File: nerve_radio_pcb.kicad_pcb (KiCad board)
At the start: 4 copper layers, 50 x 50 mm, 24 parts, among them J1 BF030-20A-B1-0360-0277-0600-LB, J2 5V GPIO Breakout, J3 3V SPI Breakout, U1 TXB0104QPWRQ1, U2 TPSM82903, U3 XBP9B-DMWT-002

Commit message: Major cleanup
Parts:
- moved J3 3.20 mm to (126.0, 103.0)
- moved U1 0.40 mm to (164.6, 106.9)
- moved J2 0.32 mm to (171.0, 109.0)
- moved TP1 0.25 mm to (169.0, 90.5)
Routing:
- net /GPIO_2/PWM_2: track 36.0 -> 33.5 mm
- net /GPIO_1/PWM_1: track 31.3 -> 28.9 mm
- net /SPI_CLK: track 24.9 -> 26.9 mm
- net /SPI_CS: track 19.2 -> 21.0 mm
- net /SPI_MOSI: track 23.3 -> 24.7 mm
- net /GPIO_2/PWM_2_{5V}: track 8.94 -> 9.75 mm
- net /SPI_MISO: track 26.6 -> 27.3 mm
- net /GPIO_1/PWM_1_{5V}: track 7.20 -> 7.89 mm
- net +5V: track 34.8 -> 35.5 mm
- net GND: vias 129 -> 121
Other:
- board text added: "3.3V"
- board text added: "5V"
- board text added: "CLK"
- board text added: "CS"
- board text added: "GND"
- board text added: "MISO"
- board text added: "MOSI"
- board text added: "PWM1_{5V}"
- board text added: "PWM2_{5V}"

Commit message: Cleanup and add battery connector
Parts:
- added J4: Battery, radio_pcb_connectors:battery, F.Cu at (167.5, 99.5)
- moved C1 2.20 mm to (163.1, 95.8)
- moved C3 2.20 mm to (168.8, 93.9)
- moved R1 2.20 mm to (166.8, 89.8)
- moved R2 2.20 mm to (166.8, 95.4)
- moved TP1 2.20 mm to (171.0, 91.4)
- moved U2 2.20 mm to (165.2, 92.5)
- moved J2 2.00 mm to (171.0, 111.0)
- moved C2 1.98 mm to (162.0, 91.0)
- moved U1 1.95 mm to (164.6, 108.8)
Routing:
- net +5V: track 35.5 -> 10.9 mm, vias 7 -> 13
- net +3V3: track 21.2 -> 18.6 mm, vias 9 -> 7
- net GND: track 10.0 -> 12.5 mm, vias 121 -> 123
- net /GPIO_2/PWM_2: track 33.5 -> 35.3 mm
- net /GPIO_1/PWM_1: track 28.9 -> 30.6 mm
- net /RADIO_UART_RX: track 26.6 -> 28.1 mm
- net /RADIO_UART_TX: track 27.9 -> 28.7 mm
- net +VSUPPLY: vias 0 -> 7
- added copper zone on F.Cu, net +3V3
- added copper zone on B.Cu, net +VSUPPLY
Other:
- board text added: "BAT+"
- board text added: "J4"

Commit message: Cleanup silkscreen
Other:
- board text added: "Daniel Jeon nerve_radio_pcb v0.1.0-alpha"
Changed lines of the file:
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@@
 	)
 	(gr_text "GND"
-		(at 172.25 99.5 90)
+		(at 172.25 99.5 -90)
 		(layer "B.SilkS" knockout)
 		(effects
@@
 	)
 	(gr_text "BAT+"
-		(at 162.75 99.5 90)
+		(at 162.75 99.5 -90)
 		(layer "B.SilkS" knockout)
 		(effects
@@
 		)
 	)
+	(gr_text "Daniel Jeon\nnerve_radio_pcb\nv0.1.0-alpha"
+		(at 148.5 128.75 0)
+		(layer "B.SilkS")
+		(effects
+			(font
+				(size 1 1)
+				(thickness 0.2)
+				(bold yes)
+			)
+			(justify bottom mirror)
+		)
+	)
 	(gr_text "3.3V"
 		(at 127.75 103 0)
@@
 	)
 	(gr_text "BAT+"
-		(at 162.75 99.5 90)
+		(at 162.75 99.5 -90)
 		(layer "F.SilkS" knockout)
 		(effects
@@
 	)
 	(gr_text "GND"
-		(at 172.25 99.5 90)
+		(at 172.25 99.5 -90)
 		(layer "F.SilkS" knockout)
 		(effects
@@
 	)
 	(via
-		(at 151 127.5)
+		(at 151.25 127.5)
 		(size 0.9)
 		(drill 0.4)
@@
 	)
 	(via
-		(at 146 127.5)
-		(size 0.9)
-		(drill 0.4)
+		(at 145.75 127.5)
+		(size 0.9)
+		(drill 0.4)

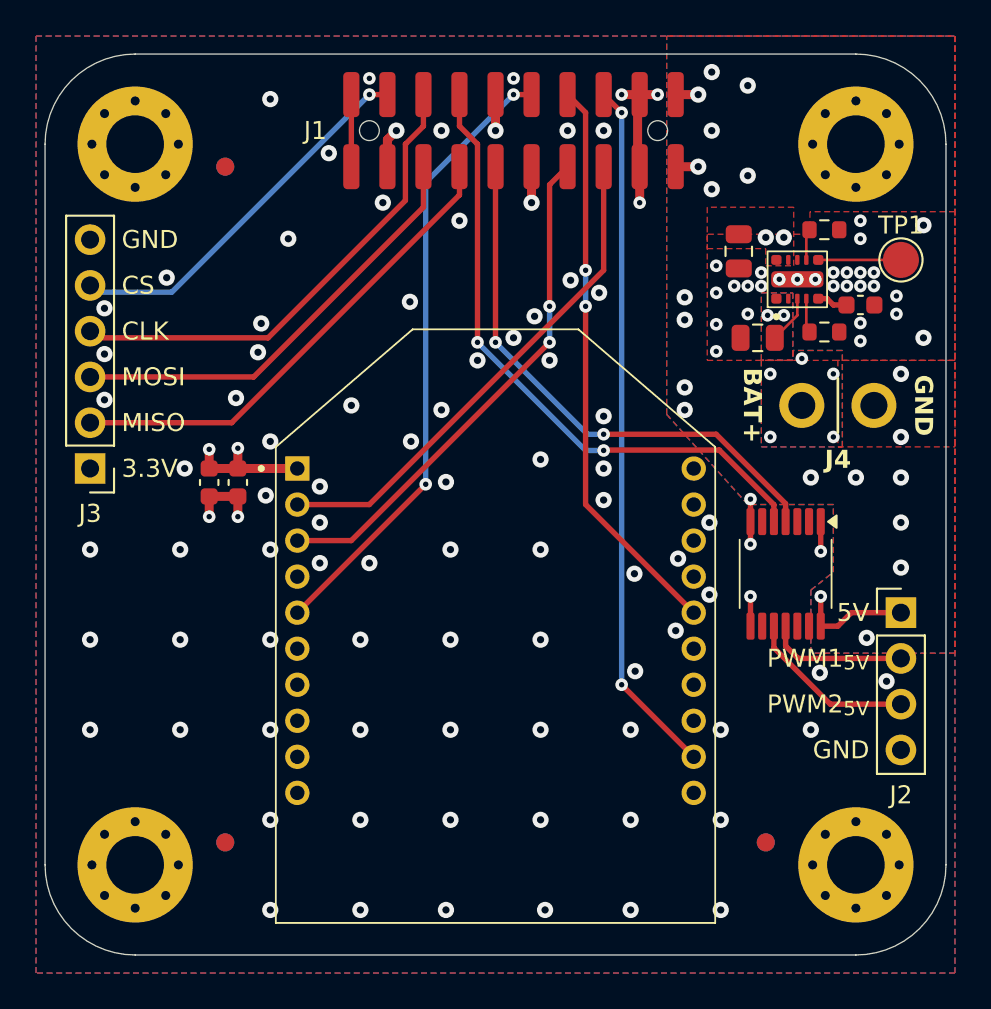
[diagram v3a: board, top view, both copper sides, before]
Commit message: Redesign layout for WIP v0.1.0
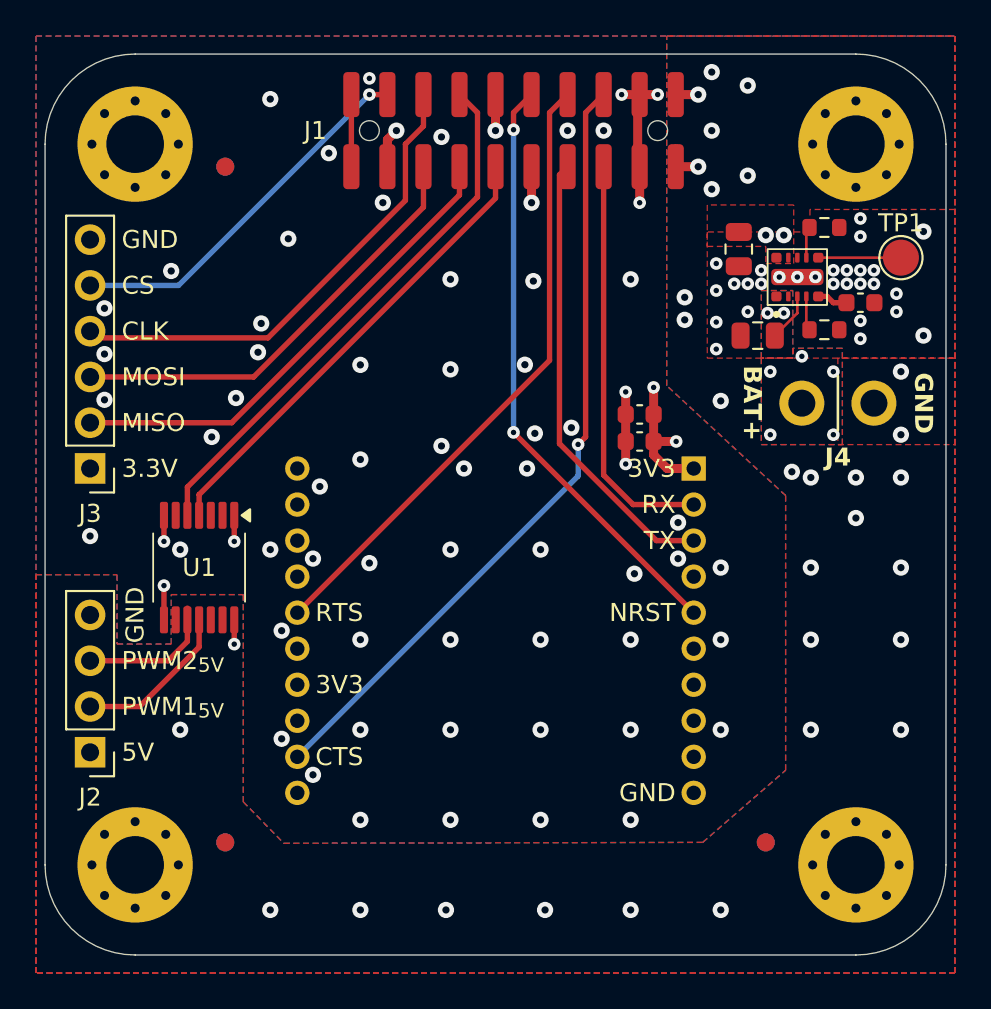
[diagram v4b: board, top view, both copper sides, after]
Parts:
- U3: moved to B.Cu
- moved J2 45.7 mm to (126.0, 118.8), turned to 180 degrees
- moved U1 32.6 mm to (132.1, 108.5)
- moved C5 24.2 mm to (156.5, 100.0), turned to 180 degrees
- moved C4 22.4 mm to (156.5, 101.5), turned to 180 degrees
- moved C1 0.12 mm to (163.1, 95.6)
- moved C2 0.12 mm to (162.0, 90.8)
- moved C3 0.12 mm to (168.8, 93.8)
- moved J4 0.12 mm to (167.5, 99.4)
- moved R1 0.12 mm to (166.8, 89.6)
- moved R2 0.12 mm to (166.8, 95.3)
- moved TP1 0.12 mm to (171.0, 91.3)
- moved U2 0.12 mm to (165.2, 92.4)
- turned U3 to 180 degrees
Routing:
- net /GPIO_2/PWM_2: track 35.3 -> 29.8 mm, vias 2 -> 0
- net /RADIO_UART_RX: track 28.1 -> 22.8 mm
- net +5V: track 10.9 -> 5.85 mm
- net /GPIO_1/PWM_1: track 30.6 -> 25.5 mm, vias 2 -> 0
- net /RADIO_UART_CTS: track 38.8 -> 43.8 mm, vias 2 -> 1
- net /RADIO_UART_TX: track 28.7 -> 25.2 mm, vias 2 -> 0
- net /RADIO_UART_RTS: track 31.6 -> 35.0 mm, vias 2 -> 0
- net /GPIO_2/PWM_2_{5V}: track 9.55 -> 7.69 mm
- net /RADIO_NRST: track 34.7 -> 33.3 mm
- net /GPIO_1/PWM_1_{5V}: track 7.79 -> 8.93 mm
- net GND: track 12.5 -> 11.7 mm, vias 123 -> 111
- net +3V3: track 18.6 -> 19.1 mm
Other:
- board text added: "3V3"
- board text added: "CTS"
- board text added: "Daniel Jeon nerve_radio_pcb v0.1.0"
- board text added: "J2"
- board text added: "J3"
- board text added: "NRST"
- board text added: "RTS"
- board text added: "RX"
- board text added: "TX"
- board text removed: "Daniel Jeon nerve_radio_pcb v0.1.0-alpha"

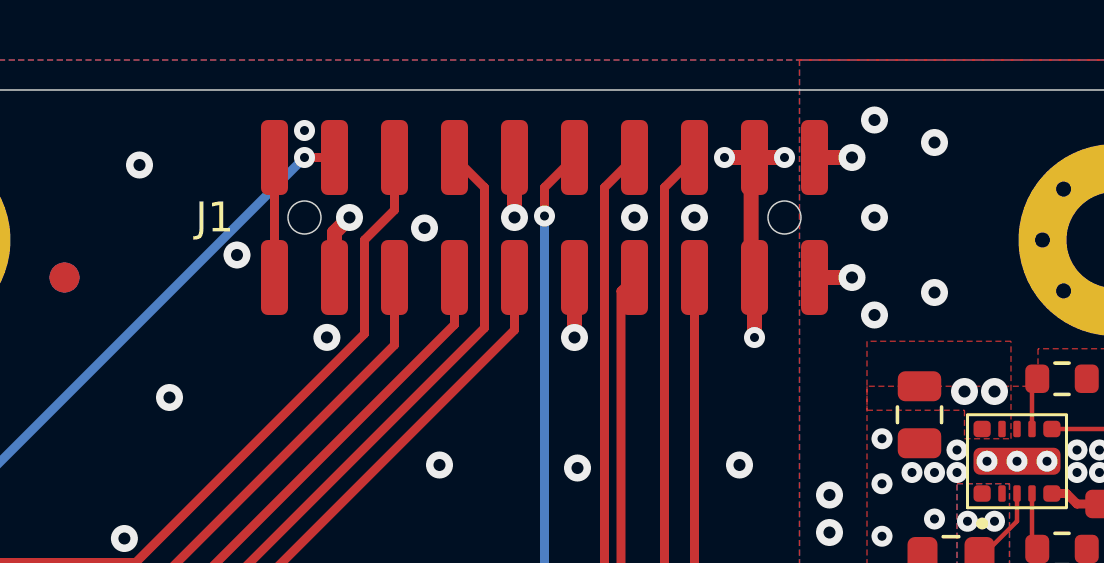
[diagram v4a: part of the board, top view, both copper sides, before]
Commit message: Fix previous bad commit 14902c5
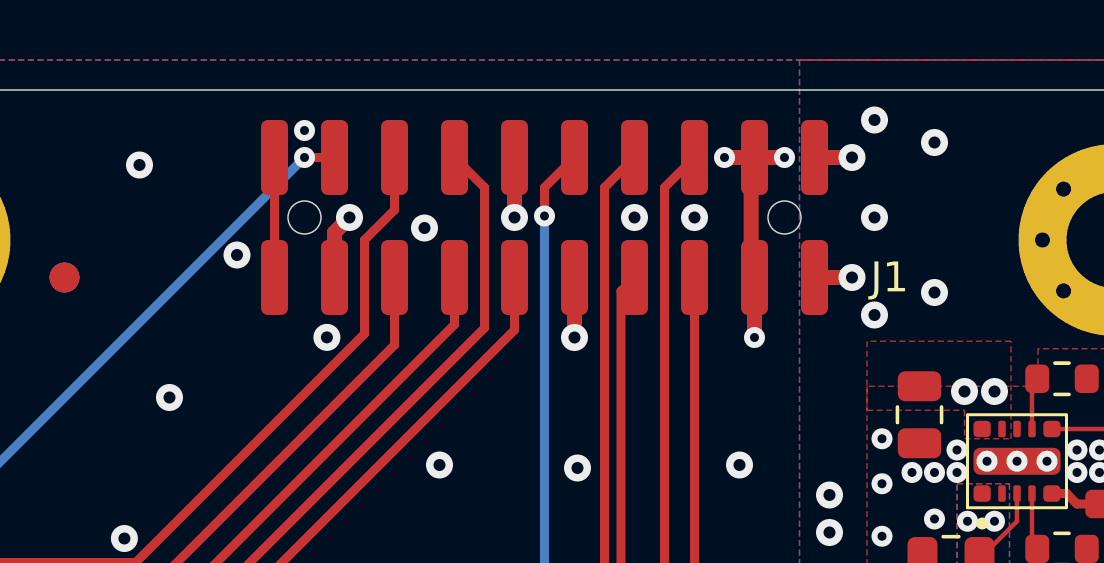
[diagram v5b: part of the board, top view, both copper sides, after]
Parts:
- J1: footprint connectors:bf030-20a-b1-0600-0277-0600-lb -> connectors:bf030-20a-b1-0360-0277-0600-lb
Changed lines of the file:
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@@
 		)
 	)
-	(footprint "connectors:bf030-20a-b1-0600-0277-0600-lb"
+	(footprint "connectors:bf030-20a-b1-0360-0277-0600-lb"
 		(layer "F.Cu")
 		(at 149.5 84.25 180)
 		(property "Reference" "J1"
-			(at 11 0 0)
+			(at -11.5 -2 0)
 			(unlocked yes)
 			(layer "F.SilkS")
@@
 		)
 		(property "Value" "BF030-20A-B1-0360-0277-0600-LB"
-			(at 0 4 0)
+			(at 0 4 180)
 			(unlocked yes)
 			(layer "F.Fab")
@@
 			)
 		)
-		(property "Footprint" "connectors:bf030-20a-b1-0600-0277-0600-lb"
+		(property "Footprint" "connectors:bf030-20a-b1-0360-0277-0600-lb"
 			(at 0 0 180)
 			(unlocked yes)
@@
 		)
 		(fp_text user "${REFERENCE}"
-			(at 0 0 0)
+			(at 0 0 180)
 			(unlocked yes)
 			(layer "F.Fab")
@@
 			(thermal_bridge_angle 45)
 		)
-		(model "${KIPRJMOD}/component_library/model_3d/gct/BF030-20A-B1-0600-0277-0600-LB.STEP"
+		(model "${KIPRJMOD}/component_library/model_3d/gct/BF030-20A-B1-0360-0277-0600-LB.STEP"
 			(offset
 				(xyz 0 0 0)
@@
 		(tags "capacitor")
 		(property "Reference" "C5"
-			(at 3.325 0 360)
+			(at 3.325 0 0)
 			(layer "F.SilkS")
 			(hide yes)
@@
 		)
 		(property "Value" "1u"
-			(at 2.5 0 360)
+			(at 2.5 0 0)
 			(layer "F.Fab")
 			(effects
@@
 		)
 		(fp_text user "${REFERENCE}"
-			(at 0 0 360)
+			(at 0 0 0)
 			(layer "F.Fab")
 			(effects
@@
 		(tags "capacitor")
 		(property "Reference" "C4"
-			(at 3.325 0 360)
+			(at 3.325 0 0)
 			(layer "F.SilkS")
 			(hide yes)
@@
 		)
 		(property "Value" "47p"
-			(at 3 0 360)
+			(at 3 0 0)
 			(layer "F.Fab")
 			(effects
@@
 		)
 		(fp_text user "${REFERENCE}"
-			(at 0 0 360)
+			(at 0 0 0)
 			(layer "F.Fab")
 			(effects

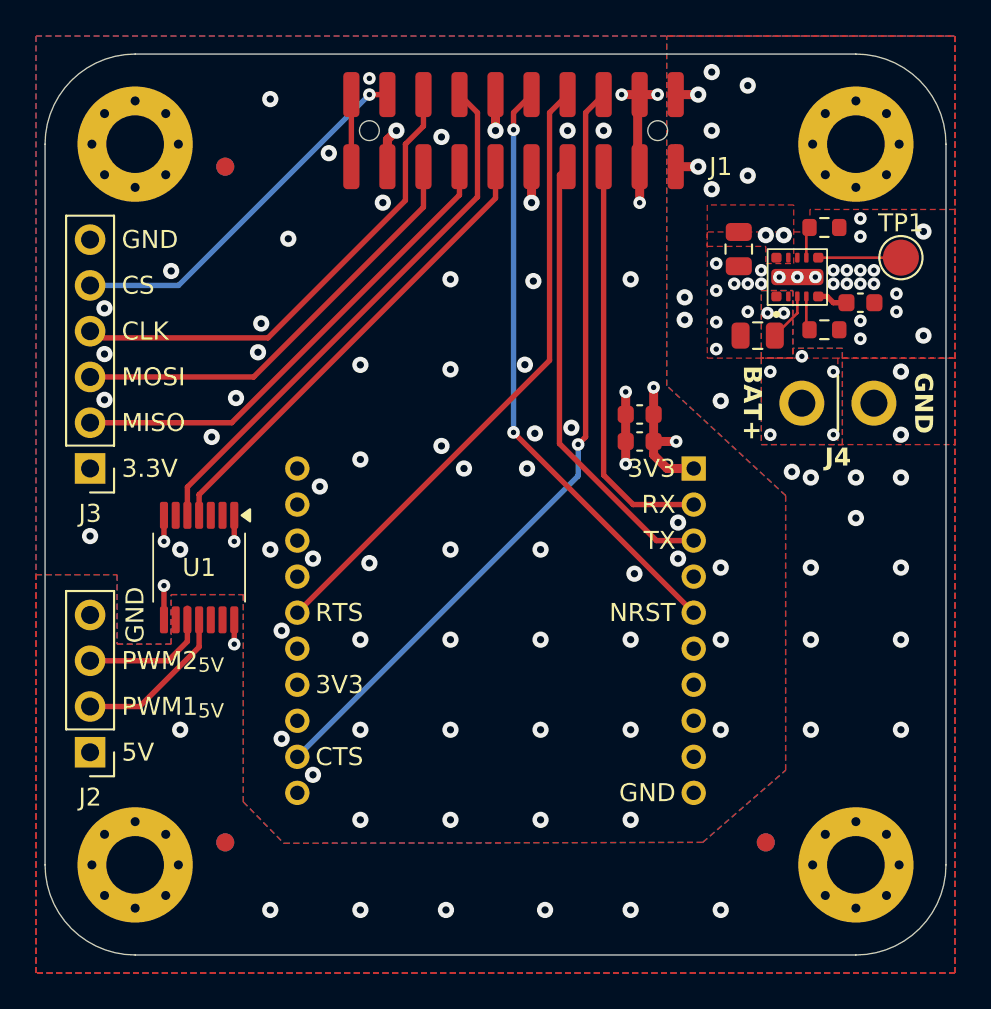
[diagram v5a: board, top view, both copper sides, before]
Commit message: Update buck converter for v1.0.0 dev
- Update component library
- Change buck regulator design to LMR51430
- Cleanup PCB
- Update version info
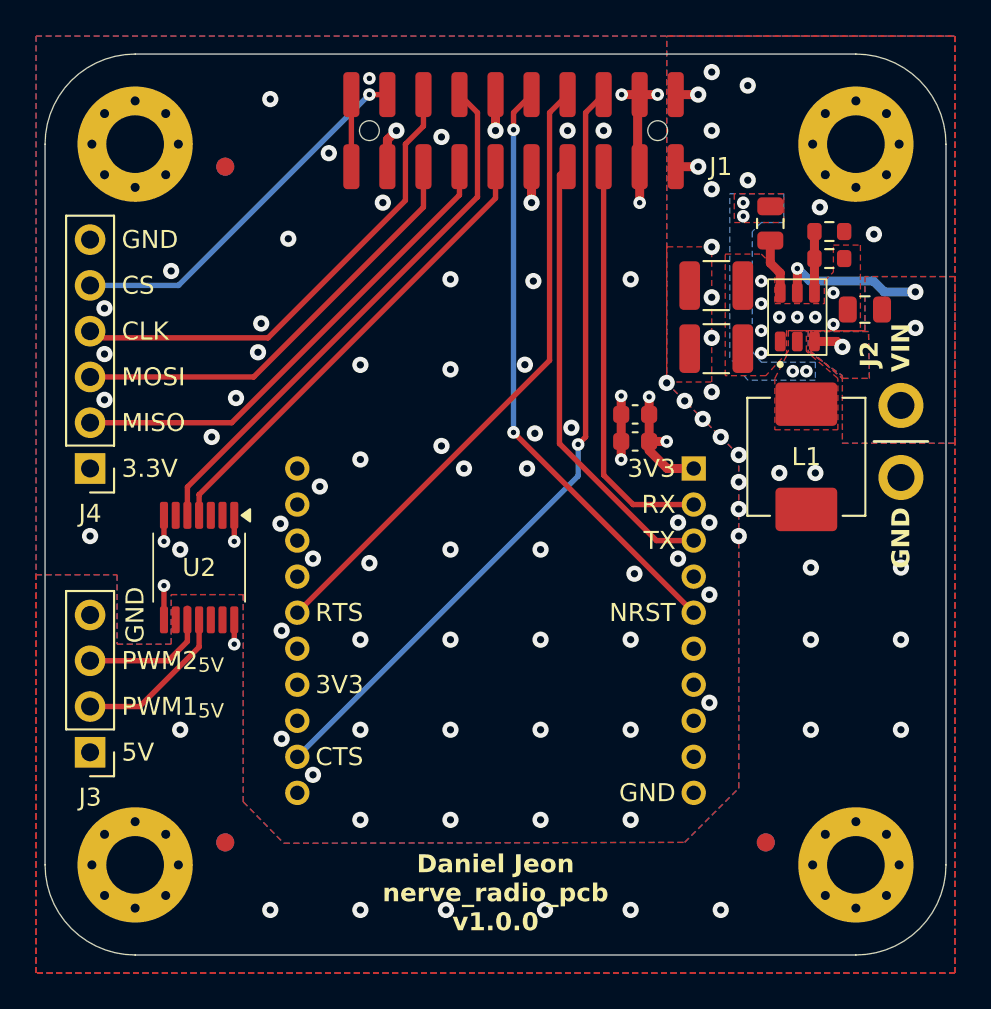
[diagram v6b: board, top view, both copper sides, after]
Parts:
- removed the J4 at (167.5, 99.4)
- removed TP1: TestPoint, TestPoint:TestPoint_Pad_D2.0mm
- removed the U2 at (165.2, 92.4)
- added C4: 22u, Capacitor_SMD:C_1210_3225Metric, F.Cu at (160.8, 96.3)
- added J2: Battery, radio_pcb_connectors:battery, F.Cu at (171.0, 101.5)
- added L1: 6u8, radio_pcb_inductors:vishay_ihlp-2525cz, F.Cu at (165.8, 102.3)
- added U1: LMR51430, ti_buck:lmr51430, F.Cu at (165.2, 94.6)
- C1: value 10u -> 100n
- C2: value 22u -> 2u2
- C3: value 16n -> 22u; footprint Capacitor_SMD:C_0603_1608Metric -> Capacitor_SMD:C_1210_3225Metric
- R1: value 76k8 -> 100k
- R2: value 76k8 -> 13k7
- moved C3 8.06 mm to (160.8, 92.8), turned to 180 degrees
- moved C2 7.76 mm to (169.0, 94.2), turned to 180 degrees
- moved C1 6.26 mm to (163.8, 89.4), turned to 90 degrees
- moved R2 3.96 mm to (167.0, 91.3)
- moved R1 0.36 mm to (167.0, 89.8)
- moved C5 0.25 mm to (156.2, 101.5)
- moved C6 0.25 mm to (156.2, 100.0)
- renumbered C4 to C5, C5 to C6, J2 to J3, J3 to J4, U1 to U2
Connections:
- C1 pad 1: +VSUPPLY -> Net-(U1-CB)
- C1 pad 2: GND -> /BUCK_SW
- C2 pad 1: +5V -> +VSUPPLY
- C3 pad 1: Net-(U2-SS/TR) -> GND
- C3 pad 2: GND -> +5V
- R1 pad 1: Net-(U2-FB/VSET) -> Net-(U1-FB)
- R1 pad 2: GND -> +5V
- R2 pad 1: Net-(U2-MODE/S-CONF) -> Net-(U1-FB)
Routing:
- net +VSUPPLY: track 2.69 -> 10.1 mm, vias 7 -> 4
- net Net-(U2-PG): track 4.59 -> 0.00 mm
- net Net-(U1-FB): track 0.00 -> 3.40 mm
- net Net-(U1-CB): track 0.00 -> 3.13 mm
- net +5V: track 5.85 -> 3.85 mm, vias 13 -> 14
- net Net-(U2-MODE/S-CONF): track 1.92 -> 0.00 mm
- net Net-(U2-FB/VSET): track 1.75 -> 0.00 mm
- net Net-(U2-SS/TR): track 1.71 -> 0.00 mm
- net +3V3: track 19.1 -> 18.4 mm
- net GND: track 11.7 -> 11.2 mm, vias 111 -> 95
- net /BUCK_SW: vias 0 -> 4
- added copper zone on B.Cu, net /BUCK_SW
- added copper zone on F.Cu, net /BUCK_SW
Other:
- board text added: "Daniel Jeon nerve_radio_pcb v1.0.0"
- board text added: "VIN"
- board text removed: "BAT+"
- board text removed: "Daniel Jeon nerve_radio_pcb v0.1.0"
- board text removed: "J4"
